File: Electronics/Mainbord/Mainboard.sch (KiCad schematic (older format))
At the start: 36 parts, among them J1 Raspberry_Pi_2_3, J2 Screw_Terminal_01x03, J3 Screw_Terminal_01x03, J4 Screw_Terminal_01x03, J5 Screw_Terminal_01x03, J6 Screw_Terminal_01x03, J7 Screw_Terminal_01x03, J8 Screw_Terminal_01x03, J9 Screw_Terminal_01x03, U1 ESP32-WROOM-32, U6 74HC4051, U7 LD1117S33TR_SOT223, U8 74HC595

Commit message: Electronics - Misc works
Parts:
- added D?: LED_Small, symbol Device:LED_Small
- added R?: 5.6, symbol Device:R_Small
- R1: value 68 -> 3.3
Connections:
- net +5V: now also D?.2 (A)
- net at C5.2, C7.2, C8.2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: now also R?.1
- new net: D?.1 (K), R?.2
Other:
- note added: "0.9mA"
- note added: "1mA\n"
- moved on the sheet: C5, C7, C8, D1, R1, U7
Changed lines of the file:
@@
 L Regulator_Linear:LD1117S33TR_SOT223 U7
 U 1 1 5DBA8842
-P 5900 3550
-F 0 "U7" H 5900 3883 50  0000 C CNN
-F 1 "LD1117S33TR_SOT223" H 5900 3792 50  0000 C CNN
-F 2 "Package_TO_SOT_SMD:SOT-223-3_TabPin2" H 5900 3750 50  0001 C CNN
-F 3 "http://www.st.com/st-web-ui/static/active/en/resource/technical/document/datasheet/CD00000544.pdf" H 6000 3300 50  0001 C CNN
-F 4 "800mA" H 5900 3701 50  0000 C CNN "Imax"
-	1    5900 3550
+P 6450 3550
+F 0 "U7" H 6450 3883 50  0000 C CNN
+F 1 "LD1117S33TR_SOT223" H 6450 3792 50  0000 C CNN
+F 2 "Package_TO_SOT_SMD:SOT-223-3_TabPin2" H 6450 3750 50  0001 C CNN
+F 3 "http://www.st.com/st-web-ui/static/active/en/resource/technical/document/datasheet/CD00000544.pdf" H 6550 3300 50  0001 C CNN
+F 4 "800mA" H 6450 3701 50  0000 C CNN "Imax"
+	1    6450 3550
 	1    0    0    -1
 $EndComp
@@
 L Device:C_Small C5
 U 1 1 5DBAA78B
-P 5400 3650
-F 0 "C5" H 5492 3696 50  0000 L CNN
-F 1 "100n" H 5492 3605 50  0000 L CNN
-F 2 "" H 5400 3650 50  0001 C CNN
-F 3 "~" H 5400 3650 50  0001 C CNN
-	1    5400 3650
+P 5950 3650
+F 0 "C5" H 6042 3696 50  0000 L CNN
+F 1 "100n" H 6042 3605 50  0000 L CNN
+F 2 "" H 5950 3650 50  0001 C CNN
+F 3 "~" H 5950 3650 50  0001 C CNN
+	1    5950 3650
 	1    0    0    -1
 $EndComp
@@
 L Device:CP_Small C8
 U 1 1 5DBAB634
-P 6750 3650
-F 0 "C8" H 6838 3696 50  0000 L CNN
-F 1 "100u" H 6838 3605 50  0000 L CNN
-F 2 "" H 6750 3650 50  0001 C CNN
-F 3 "~" H 6750 3650 50  0001 C CNN
-	1    6750 3650
+P 7300 3650
+F 0 "C8" H 7388 3696 50  0000 L CNN
+F 1 "100u" H 7388 3605 50  0000 L CNN
+F 2 "" H 7300 3650 50  0001 C CNN
+F 3 "~" H 7300 3650 50  0001 C CNN
+	1    7300 3650
 	1    0    0    -1
 $EndComp
@@
 L Device:LED_Small D1
 U 1 1 5DBAC806
-P 7050 3550
-F 0 "D1" H 7050 3785 50  0000 C CNN
-F 1 "LED_Small" H 7050 3694 50  0000 C CNN
-F 2 "" V 7050 3550 50  0001 C CNN
-F 3 "~" V 7050 3550 50  0001 C CNN
-	1    7050 3550
+P 7600 3550
+F 0 "D1" H 7600 3700 50  0000 C CNN
+F 1 "LED_Small" H 7600 3694 50  0001 C CNN
+F 2 "" V 7600 3550 50  0001 C CNN
+F 3 "~" V 7600 3550 50  0001 C CNN
+	1    7600 3550
 	-1   0    0    -1
 $EndComp
@@
 L Device:R_Small R1
 U 1 1 5DBAE1BE
-P 7150 3700
-F 0 "R1" H 7209 3746 50  0000 L CNN
-F 1 "68" H 7209 3655 50  0000 L CNN
-F 2 "" H 7150 3700 50  0001 C CNN
-F 3 "~" H 7150 3700 50  0001 C CNN
-	1    7150 3700
+P 7700 3700
+F 0 "R1" H 7759 3746 50  0000 L CNN
+F 1 "3.3" H 7759 3655 50  0000 L CNN
+F 2 "" H 7700 3700 50  0001 C CNN
+F 3 "~" H 7700 3700 50  0001 C CNN
+	1    7700 3700
 	1    0    0    -1
 $EndComp
 Wire Wire Line
-	5600 3550 5400 3550
+	6150 3550 5950 3550
 Wire Wire Line
-	5400 3750 5400 3850
+	5950 3750 5950 3850
 Wire Wire Line
-	5400 3850 5900 3850
+	5950 3850 6450 3850
 Wire Wire Line
-	5900 3850 6350 3850
-Connection ~ 5900 3850
+	6450 3850 6900 3850
+Connection ~ 6450 3850
 Wire Wire Line
-	6350 3850 6750 3850
+	6900 3850 7300 3850
 Wire Wire Line
-	6750 3850 6750 3750
-Connection ~ 6350 3850
+	7300 3850 7300 3750
+Connection ~ 6900 3850
 Wire Wire Line
-	6200 3550 6350 3550
-Connection ~ 6350 3550
+	6750 3550 6900 3550
+Connection ~ 6900 3550
 Wire Wire Line
-	6350 3550 6550 3550
+	6900 3550 7100 3550
 Wire Wire Line
-	6350 3850 6350 3750
+	6900 3850 6900 3750
 $Comp
 L Device:C_Small C7
 U 1 1 5DBAAEF4
-P 6350 3650
-F 0 "C7" H 6442 3696 50  0000 L CNN
-F 1 "100n" H 6442 3605 50  0000 L CNN
-F 2 "" H 6350 3650 50  0001 C CNN
-F 3 "~" H 6350 3650 50  0001 C CNN
-	1    6350 3650
+P 6900 3650
+F 0 "C7" H 6992 3696 50  0000 L CNN
+F 1 "100n" H 6992 3605 50  0000 L CNN
+F 2 "" H 6900 3650 50  0001 C CNN
+F 3 "~" H 6900 3650 50  0001 C CNN
+	1    6900 3650
 	1    0    0    -1
 $EndComp
 Wire Wire Line
-	6750 3550 6950 3550
-Connection ~ 6750 3550
+	7300 3550 7500 3550
+Connection ~ 7300 3550
 Wire Wire Line
-	7150 3550 7150 3600
+	7700 3550 7700 3600
 Wire Wire Line
-	7150 3800 7150 3850
+	7700 3800 7700 3850
 Wire Wire Line
-	7150 3850 6750 3850
-Connection ~ 6750 3850
+	7700 3850 7300 3850
+Connection ~ 7300 3850
 $Comp
 L power:+5V #PWR0150
 U 1 1 5DBCAFCB
-P 5400 3550
-F 0 "#PWR0150" H 5400 3400 50  0001 C CNN
-F 1 "+5V" H 5415 3723 50  0000 C CNN
-F 2 "" H 5400 3550 50  0001 C CNN
-F 3 "" H 5400 3550 50  0001 C CNN
-	1    5400 3550
+P 5950 3550
+F 0 "#PWR0150" H 5950 3400 50  0001 C CNN
+F 1 "+5V" H 5965 3723 50  0000 C CNN
+F 2 "" H 5950 3550 50  0001 C CNN
+F 3 "" H 5950 3550 50  0001 C CNN
+	1    5950 3550
 	1    0    0    -1
 $EndComp
-Connection ~ 5400 3550
+Connection ~ 5950 3550
 $Comp
 L power:+3.3V #PWR0151
 U 1 1 5DBCB934
-P 6550 3550
-F 0 "#PWR0151" H 6550 3400 50  0001 C CNN
-F 1 "+3.3V" H 6565 3723 50  0000 C CNN
-F 2 "" H 6550 3550 50  0001 C CNN
-F 3 "" H 6550 3550 50  0001 C CNN
-	1    6550 3550
+P 7100 3550
+F 0 "#PWR0151" H 7100 3400 50  0001 C CNN
+F 1 "+3.3V" H 7115 3723 50  0000 C CNN
+F 2 "" H 7100 3550 50  0001 C CNN
+F 3 "" H 7100 3550 50  0001 C CNN
+	1    7100 3550
 	1    0    0    -1
 $EndComp
-Connection ~ 6550 3550
+Connection ~ 7100 3550
 Wire Wire Line
-	6550 3550 6750 3550
-Text Notes 5400 4100 0    50   ~ 0
+	7100 3550 7300 3550
+Text Notes 5950 4100 0    50   ~ 0
 3.3V generation\ncheck if 800 mA is enough
 Text GLabel 3200 1650 0    50   Input ~ 0
@@
 EndData
 $EndBitmap
+$Comp
+L Device:LED_Small D?
+U 1 1 5DF44451
+P 5750 3550
+F 0 "D?" H 5750 3450 50  0000 C CNN
+F 1 "LED_Small" H 5750 3450 50  0001 C CNN
+F 2 "" V 5750 3550 50  0001 C CNN
+F 3 "~" V 5750 3550 50  0001 C CNN
+	1    5750 3550
+	1    0    0    1
+$EndComp
+$Comp
+L Device:R_Small R?
+U 1 1 5DF44458
+P 5600 3700
+F 0 "R?" H 5659 3746 50  0000 L CNN
+F 1 "5.6" H 5659 3655 50  0000 L CNN
+F 2 "" H 5600 3700 50  0001 C CNN
+F 3 "~" H 5600 3700 50  0001 C CNN
+	1    5600 3700
+	-1   0    0    1
+$EndComp
+Wire Wire Line
+	5650 3550 5600 3550
+Wire Wire Line
+	5600 3550 5600 3600
+Wire Wire Line
+	5600 3800 5600 3850
+Wire Wire Line
+	5600 3850 5950 3850
+Connection ~ 5950 3850
+Wire Wire Line
+	5950 3550 5850 3550
+Text Notes 7700 3550 0    50   ~ 0
+1mA\n
+Text Notes 5450 3550 0    50   ~ 0
+0.9mA
 $EndSCHEMATC

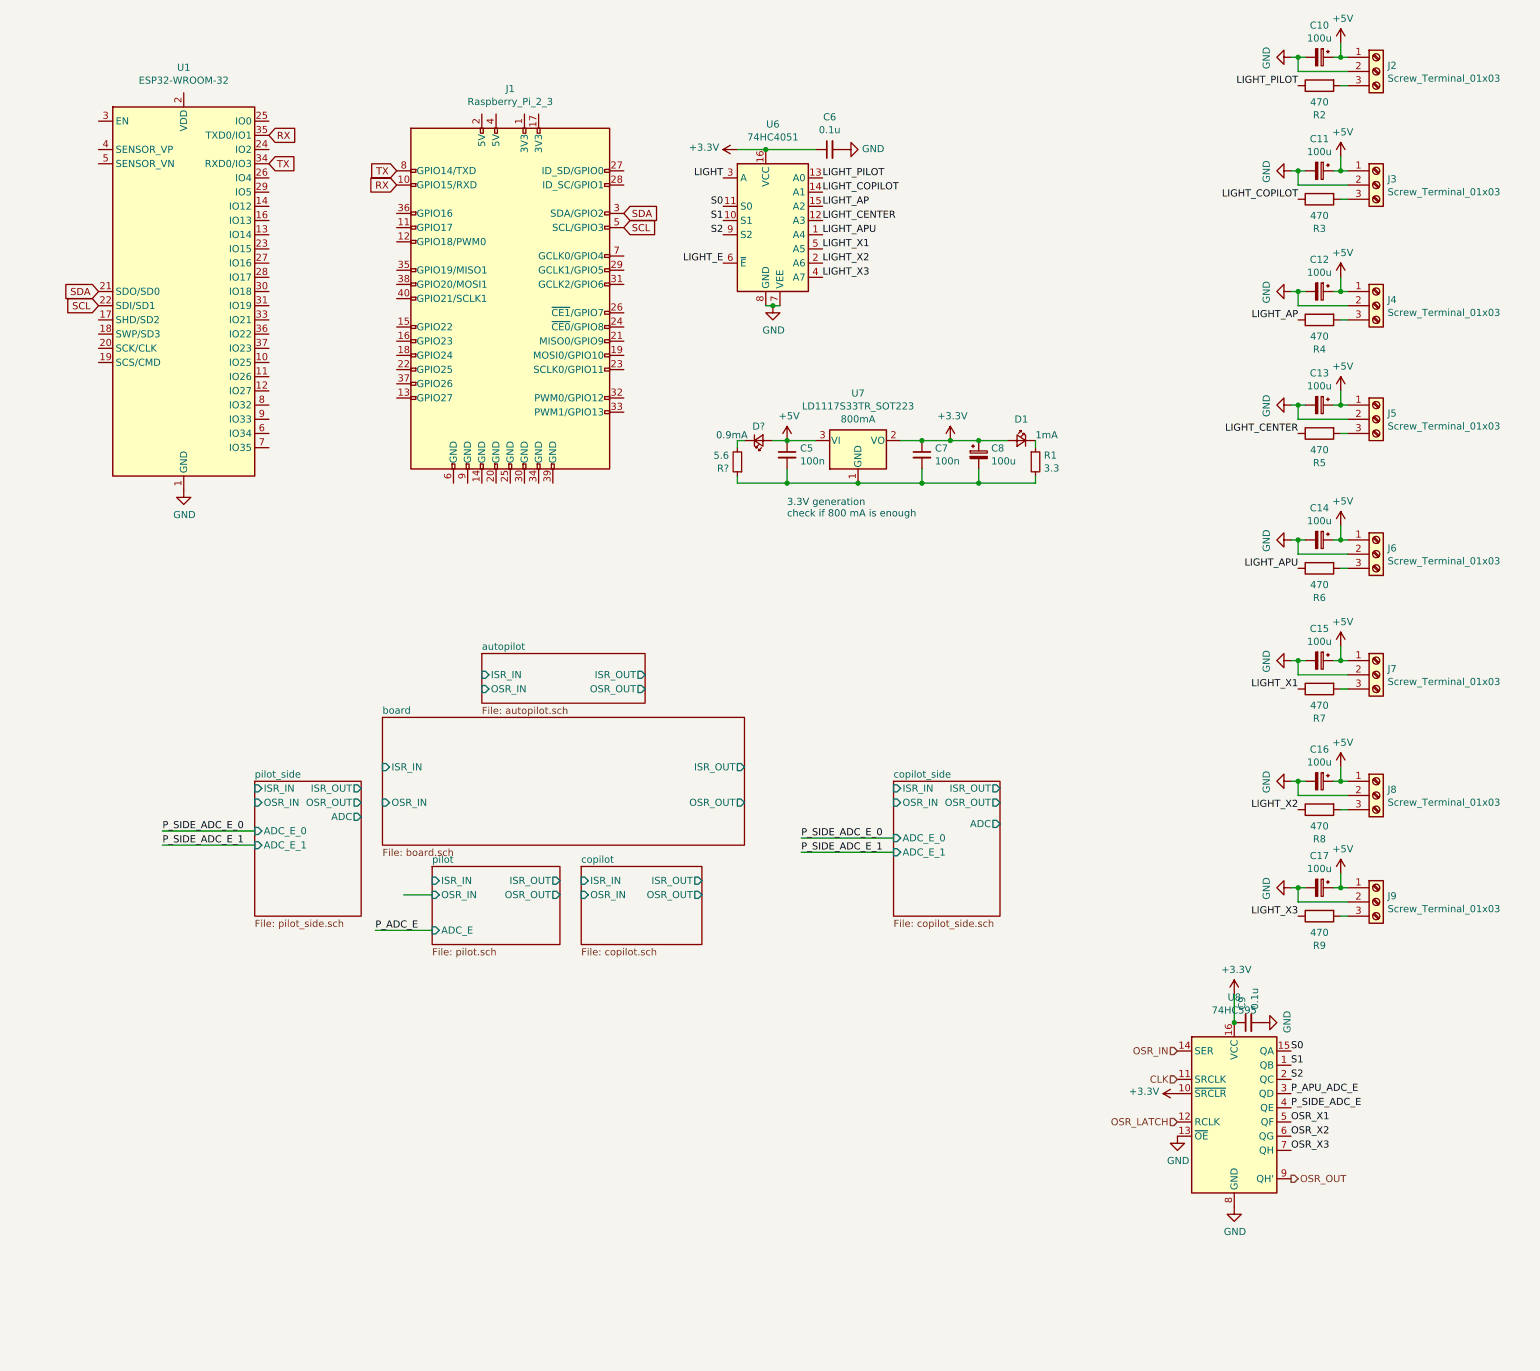
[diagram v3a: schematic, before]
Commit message: Electronics - Adds LCSC part numbers and footprints
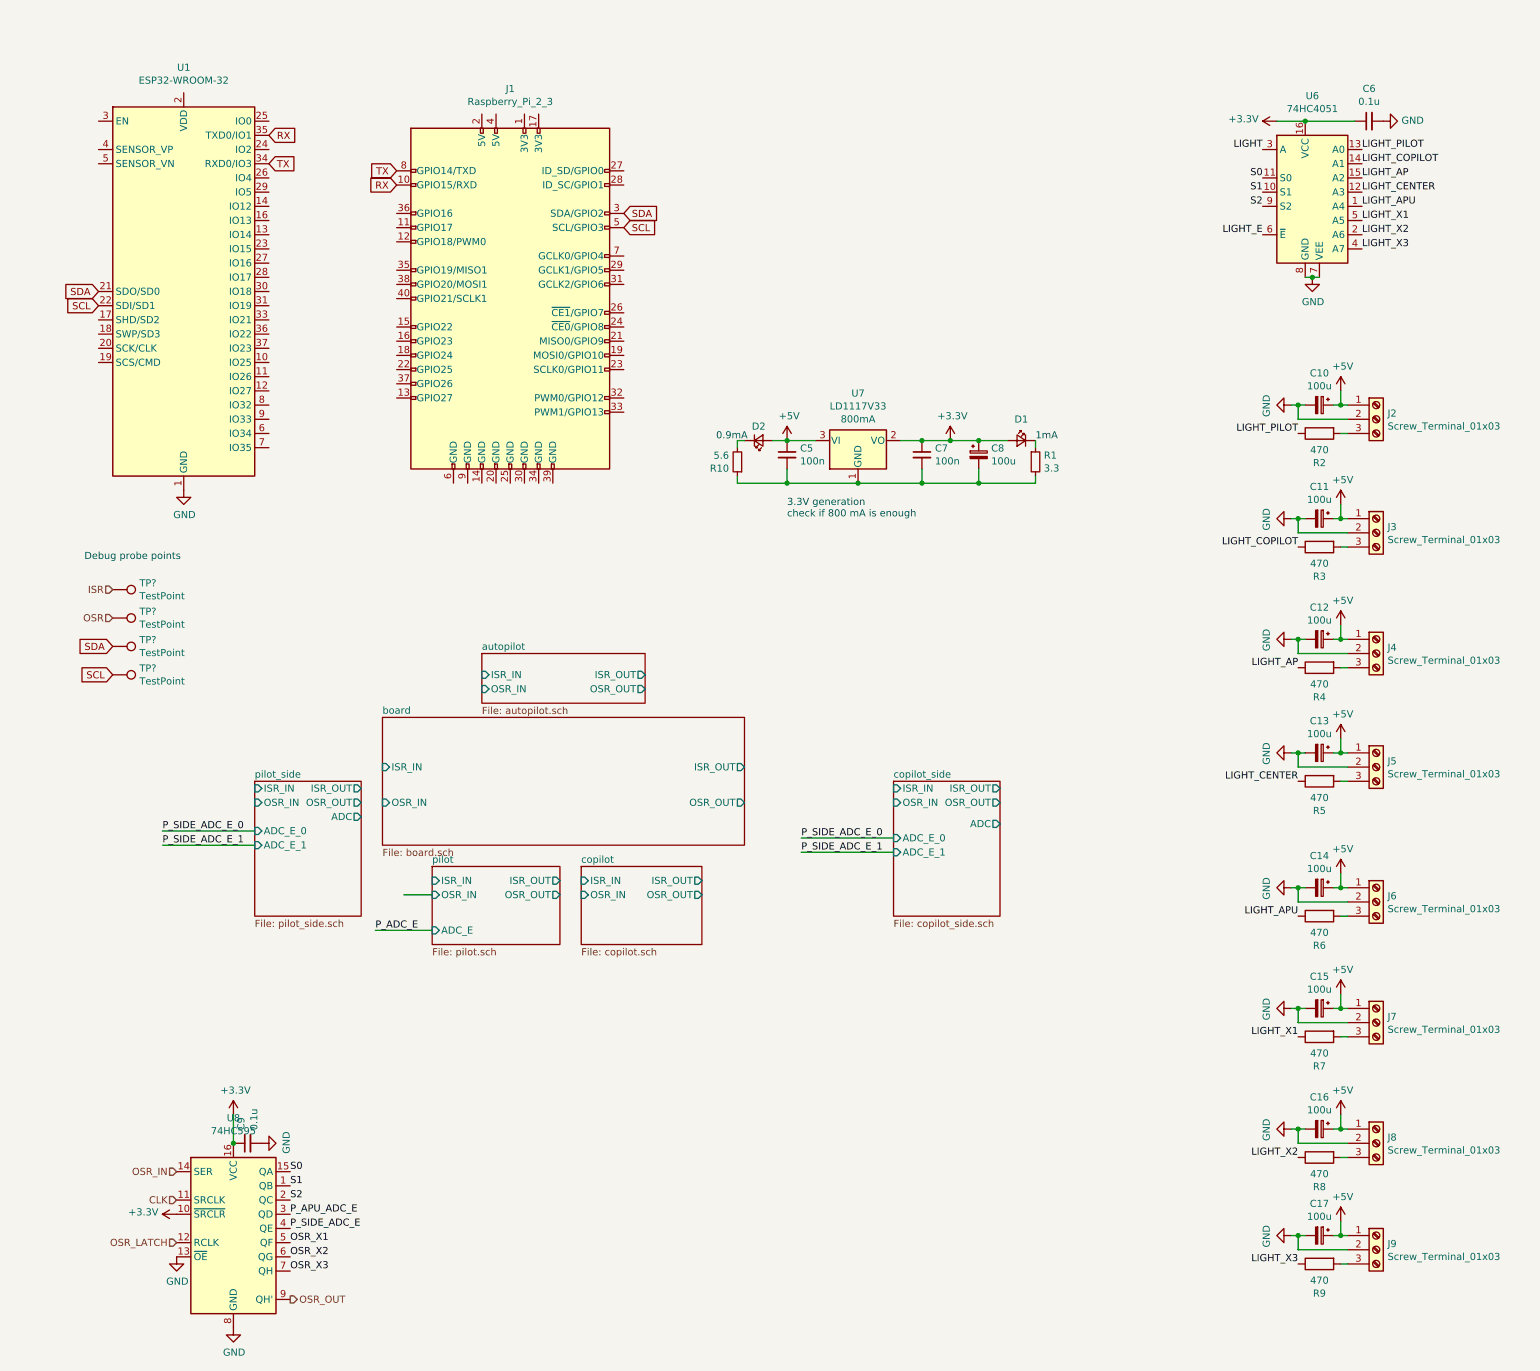
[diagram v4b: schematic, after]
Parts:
- added TP? (x4): TestPoint, symbol Connector:TestPoint
- D1: footprint (none) -> LED_SMD:LED_0805_2012Metric; LCSC (none) -> C84256
- D2: renamed from D?; footprint (none) -> LED_SMD:LED_0805_2012Metric; LCSC (none) -> C84256
- U7: value LD1117S33TR_SOT223 -> LD1117V33; footprint Package_TO_SOT_SMD:SOT-223-3_TabPin2 -> Package_TO_SOT_THT:TO-220-3_Horizontal_TabDown
- gave numbers to parts that had none: 1
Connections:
- net SCL: now also TP?.1
- net SDA: now also TP?.1
- new net ISR: TP?.1
- new net OSR: TP?.1
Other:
- note added: "Debug probe points"
- moved on the sheet: C10, C11, C12, C13, C14, C15, C16, C17, C6, C9, J2, J3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
